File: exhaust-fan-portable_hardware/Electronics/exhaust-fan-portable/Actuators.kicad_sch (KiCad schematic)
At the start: 4 parts, among them Q1 NMOS, Q2 NMOS, U2 LM741, U3 LM741

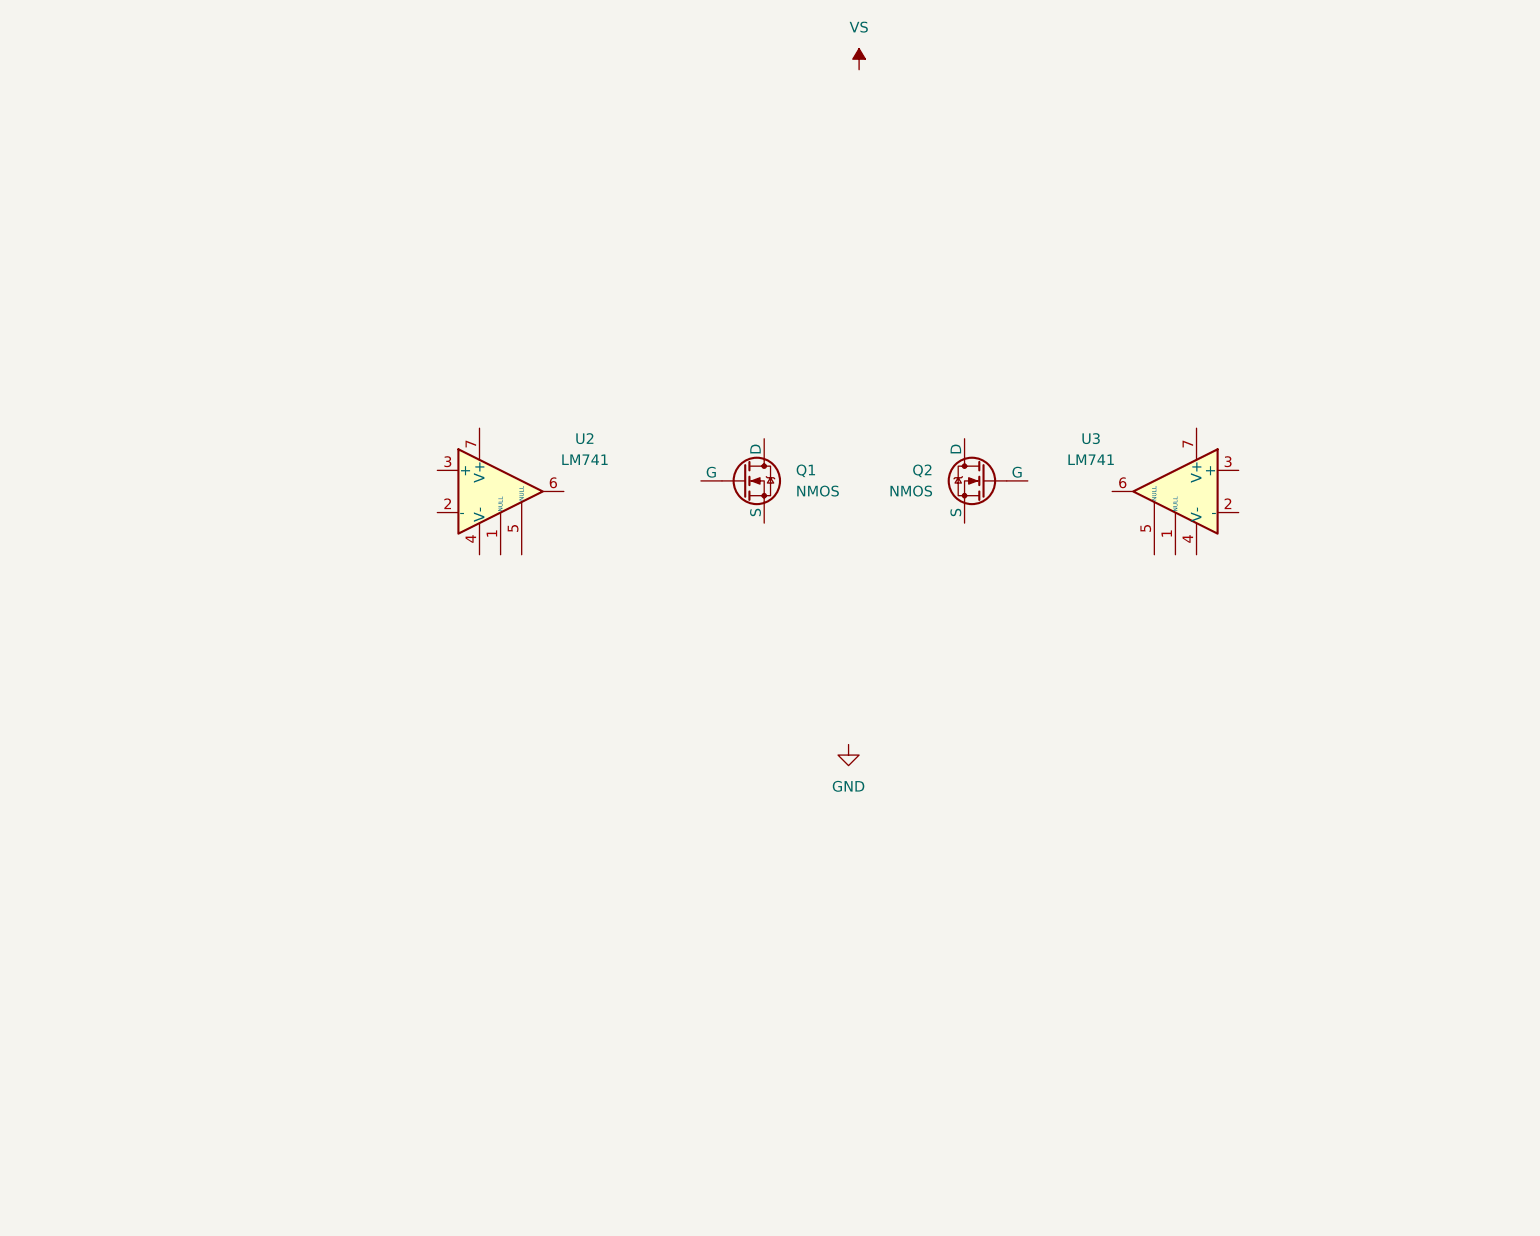
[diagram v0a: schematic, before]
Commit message: layed out rough schematic and added sensor comparison
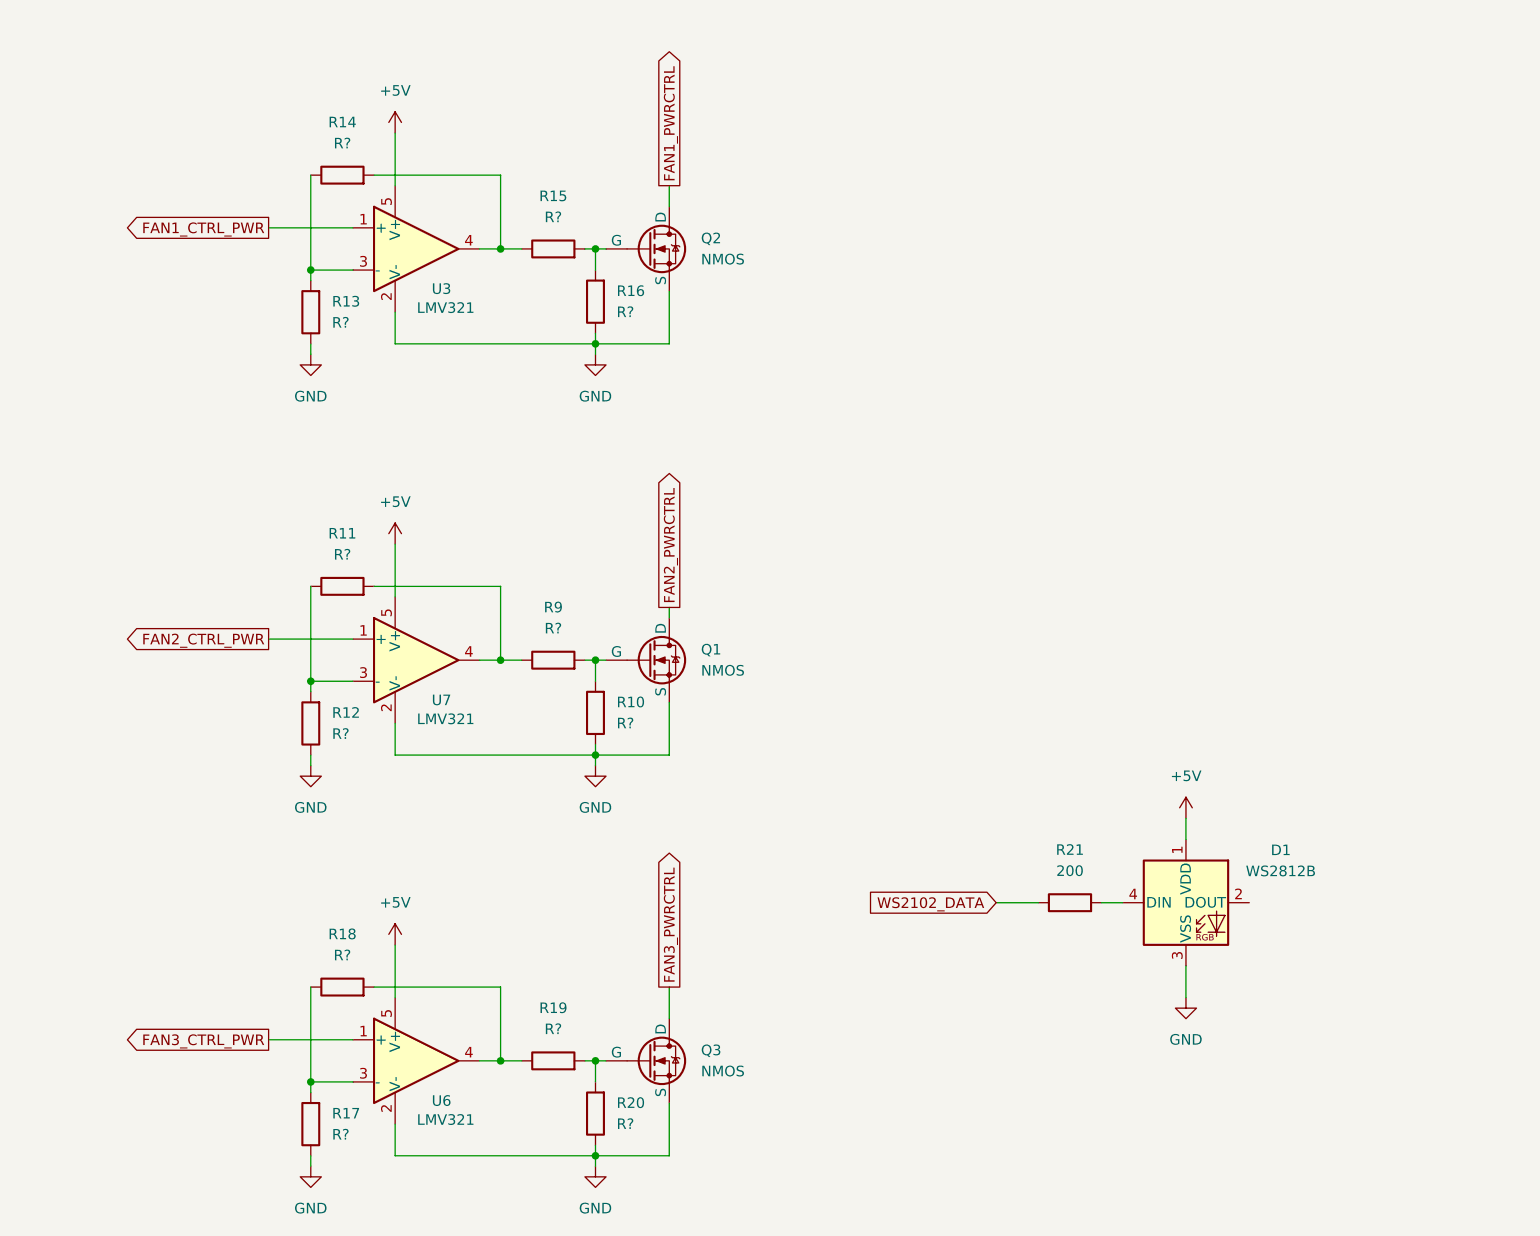
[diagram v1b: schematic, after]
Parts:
- removed U2, U3: LM741, symbol Amplifier_Operational:LM741
- added D1: WS2812B, LED_SMD:LED_WS2812B_PLCC4_5.0x5.0mm_P3.2mm, symbol LED:WS2812B
- added Q3: NMOS, symbol Simulation_SPICE:NMOS
- added R10, R11, R12, R13, R14, R15, R16, R17, R18, R19, R20, R9: R?, symbol Device:R
- added R21: 200, symbol Device:R
- added U3, U6, U7: LMV321, symbol Amplifier_Operational:LMV321
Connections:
- net GND: now also Q1.3 (S), Q2.3 (S), D1.3 (VSS), Q3.3 (S), R10.1, R12.1, R13.1, R16.1, R17.1, R20.1, U3.2 (V-), U6.2 (V-), U7.2 (V-)
- net FAN1_PWRCTRL: now reaches Q2.1 (D)
- net at Q2.2 (G): now also R15.2, R16.2
- net FAN2_PWRCTRL: now reaches Q1.1 (D)
- net at Q1.2 (G): now also R10.2, R9.2
- new net: R11.1, R12.2, U7.3 (-)
- new net: R11.2, R9.1, U7.4
- new net: Q3.2 (G), R19.2, R20.2
- new net: D1.4 (DIN), R21.2
- new net: R13.2, R14.1, U3.3 (-)
- new net: R14.2, R15.1, U3.4
- new net: R17.2, R18.1, U6.3 (-)
- new net: R18.2, R19.1, U6.4
- new net +5V: D1.1 (VDD), U3.5 (V+), U6.5 (V+), U7.5 (V+)
- new net FAN1_CTRL_PWR: U3.1 (+)
- new net FAN2_CTRL_PWR: U7.1 (+)
- new net FAN3_CTRL_PWR: U6.1 (+)
- new net FAN3_PWRCTRL: Q3.1 (D)
- new net WS2102_DATA: R21.1
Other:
- moved on the sheet: Q1

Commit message: fixed case design
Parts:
- Q1, Q2, Q3: footprint (none) -> Package_TO_SOT_SMD:TO-263-2
- R10, R16, R20: value R? -> 10K; footprint (none) -> Resistor_SMD:R_0603_1608Metric_Pad0.98x0.95mm_HandSolder
- R11, R14, R18: value R? -> 50K; footprint (none) -> Resistor_SMD:R_0603_1608Metric_Pad0.98x0.95mm_HandSolder
- R12, R13, R17: value R? -> 5K; footprint (none) -> Resistor_SMD:R_0603_1608Metric_Pad0.98x0.95mm_HandSolder
- R15, R19, R9: value R? -> 470; footprint (none) -> Resistor_SMD:R_1206_3216Metric_Pad1.30x1.75mm_HandSolder
- R21: footprint (none) -> Resistor_SMD:R_1206_3216Metric_Pad1.30x1.75mm_HandSolder
- U3, U6, U7: footprint (none) -> Package_SO:SO-6_4.4x3.6mm_P1.27mm
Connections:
- no-connect marks 0 -> 1
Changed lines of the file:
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@@
 		(color 0 0 0 0)
 	)
+	(no_connect
+		(at 171.45 134.62)
+	)
 	(wire
 		(pts
@@
 	(wire
 		(pts
-			(xy 53.34 151.13) (xy 63.5 151.13)
+			(xy 43.18 151.13) (xy 63.5 151.13)
 		)
 		(stroke
@@
 	(wire
 		(pts
-			(xy 53.34 53.34) (xy 63.5 53.34)
+			(xy 43.18 53.34) (xy 63.5 53.34)
 		)
 		(stroke
@@
 	(wire
 		(pts
-			(xy 53.34 102.87) (xy 63.5 102.87)
+			(xy 43.18 102.87) (xy 63.5 102.87)
 		)
 		(stroke
@@
 	(global_label "FAN1_CTRL_PWR"
 		(shape output)
-		(at 53.34 53.34 180)
+		(at 43.18 53.34 180)
 		(fields_autoplaced yes)
 		(effects
@@
 		)
 		(property "Intersheetrefs" "${INTERSHEET_REFS}"
-			(at 35.1753 53.34 0)
+			(at 25.0153 53.34 0)
 			(effects
 				(font
@@
 	(global_label "FAN2_CTRL_PWR"
 		(shape output)
-		(at 53.34 102.87 180)
+		(at 43.18 102.87 180)
 		(fields_autoplaced yes)
 		(effects
@@
 		)
 		(property "Intersheetrefs" "${INTERSHEET_REFS}"
-			(at 35.1753 102.87 0)
+			(at 25.0153 102.87 0)
 			(effects
 				(font
@@
 	(global_label "FAN3_CTRL_PWR"
 		(shape output)
-		(at 53.34 151.13 180)
+		(at 43.18 151.13 180)
 		(fields_autoplaced yes)
 		(effects
@@
 		)
 		(property "Intersheetrefs" "${INTERSHEET_REFS}"
-			(at 35.1753 151.13 0)
+			(at 25.0153 151.13 0)
 			(effects
 				(font
@@
 			)
 		)
-		(property "Footprint" ""
+		(property "Footprint" "Package_SO:SO-6_4.4x3.6mm_P1.27mm"
 			(at 71.12 105.41 0)
 			(effects
@@
 			)
 		)
-		(property "Footprint" ""
+		(property "Footprint" "Package_TO_SOT_SMD:TO-263-2"
 			(at 104.14 151.13 0)
 			(effects
@@
 			)
 		)
-		(property "Value" "R?"
+		(property "Value" "5K"
 			(at 60.96 114.2999 0)
 			(effects
@@
 			)
 		)
-		(property "Footprint" ""
+		(property "Footprint" "Resistor_SMD:R_0603_1608Metric_Pad0.98x0.95mm_HandSolder"
 			(at 60.198 113.03 90)
 			(effects
@@
 			)
 		)
-		(property "Footprint" ""
+		(property "Footprint" "Resistor_SMD:R_1206_3216Metric_Pad1.30x1.75mm_HandSolder"
 			(at 149.86 136.398 90)
 			(effects
@@
 			)
 		)
-		(property "Value" "R?"
+		(property "Value" "10K"
 			(at 95.25 161.2899 0)
 			(effects
@@
 			)
 		)
-		(property "Footprint" ""
+		(property "Footprint" "Resistor_SMD:R_0603_1608Metric_Pad0.98x0.95mm_HandSolder"
 			(at 94.488 160.02 90)
 			(effects
@@
 			)
 		)
-		(property "Value" "R?"
+		(property "Value" "50K"
 			(at 62.23 92.71 90)
 			(effects
@@
 			)
 		)
-		(property "Footprint" ""
+		(property "Footprint" "Resistor_SMD:R_0603_1608Metric_Pad0.98x0.95mm_HandSolder"
 			(at 62.23 98.298 90)
 			(effects
@@
 			)
 		)
-		(property "Value" "R?"
+		(property "Value" "50K"
 			(at 62.23 43.18 90)
 			(effects
@@
 			)
 		)
-		(property "Footprint" ""
+		(property "Footprint" "Resistor_SMD:R_0603_1608Metric_Pad0.98x0.95mm_HandSolder"
 			(at 62.23 48.768 90)
 			(effects
@@
 			)
 		)
-		(property "Value" "R?"
+		(property "Value" "10K"
 			(at 95.25 113.0299 0)
 			(effects
@@
 			)
 		)
-		(property "Footprint" ""
+		(property "Footprint" "Resistor_SMD:R_0603_1608Metric_Pad0.98x0.95mm_HandSolder"
 			(at 94.488 111.76 90)
 			(effects
@@
 			)
 		)
-		(property "Footprint" ""
+		(property "Footprint" "Package_TO_SOT_SMD:TO-263-2"
 			(at 104.14 102.87 0)
 			(effects
@@
 			)
 		)
-		(property "Footprint" ""
+		(property "Footprint" "Package_SO:SO-6_4.4x3.6mm_P1.27mm"
 			(at 71.12 153.67 0)
 			(effects
@@
 			)
 		)
-		(property "Value" "R?"
+		(property "Value" "470"
 			(at 87.63 149.86 90)
 			(effects
@@
 			)
 		)
-		(property "Footprint" ""
+		(property "Footprint" "Resistor_SMD:R_1206_3216Metric_Pad1.30x1.75mm_HandSolder"
 			(at 87.63 155.448 90)
 			(effects
@@
 			)
 		)
-		(property "Footprint" ""
+		(property "Footprint" "Package_TO_SOT_SMD:TO-263-2"
 			(at 104.14 53.34 0)
 			(effects
@@
 			)
 		)
-		(property "Value" "R?"
+		(property "Value" "50K"
 			(at 62.23 140.97 90)
 			(effects
@@
 			)
 		)
-		(property "Footprint" ""
+		(property "Footprint" "Resistor_SMD:R_0603_1608Metric_Pad0.98x0.95mm_HandSolder"
 			(at 62.23 146.558 90)
 			(effects
@@
 			)
 		)
-		(property "Value" "R?"
+		(property "Value" "470"
 			(at 87.63 101.6 90)
 			(effects
@@
 			)
 		)
-		(property "Footprint" ""
+		(property "Footprint" "Resistor_SMD:R_1206_3216Metric_Pad1.30x1.75mm_HandSolder"
 			(at 87.63 107.188 90)
 			(effects
@@
 			)
 		)
-		(property "Value" "R?"
+		(property "Value" "5K"
 			(at 60.96 162.5599 0)
 			(effects
@@
 			)
 		)
-		(property "Footprint" ""
+		(property "Footprint" "Resistor_SMD:R_0603_1608Metric_Pad0.98x0.95mm_HandSolder"
 			(at 60.198 161.29 90)
 			(effects
@@
 			)
 		)
-		(property "Value" "R?"
+		(property "Value" "470"
 			(at 87.63 52.07 90)
 			(effects
@@
 			)
 		)
-		(property "Footprint" ""
+		(property "Footprint" "Resistor_SMD:R_1206_3216Metric_Pad1.30x1.75mm_HandSolder"
 			(at 87.63 57.658 90)
 			(effects
@@
 			)
 		)
-		(property "Value" "R?"
+		(property "Value" "5K"
 			(at 60.96 64.7699 0)
 			(effects
@@
 			)
 		)
-		(property "Footprint" ""
+		(property "Footprint" "Resistor_SMD:R_0603_1608Metric_Pad0.98x0.95mm_HandSolder"
 			(at 60.198 63.5 90)
 			(effects
@@
 			)
 		)
-		(property "Footprint" ""
+		(property "Footprint" "Package_SO:SO-6_4.4x3.6mm_P1.27mm"
 			(at 71.12 55.88 0)
 			(effects
@@
 			)
 		)
-		(property "Value" "R?"
+		(property "Value" "10K"
 			(at 95.25 63.4999 0)
 			(effects
@@
 			)
 		)
-		(property "Footprint" ""
+		(property "Footprint" "Resistor_SMD:R_0603_1608Metric_Pad0.98x0.95mm_HandSolder"
 			(at 94.488 62.23 90)
 			(effects
